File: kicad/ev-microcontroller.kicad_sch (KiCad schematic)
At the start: 0 parts

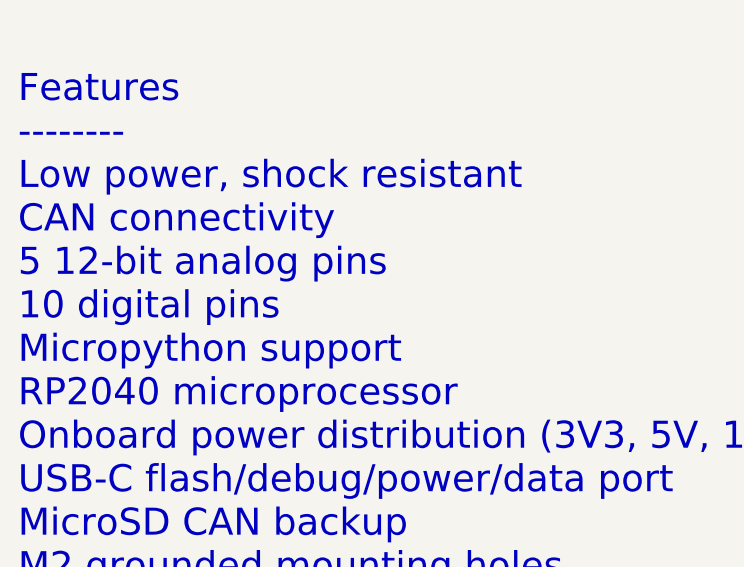
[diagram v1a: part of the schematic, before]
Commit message: Updated schematic with various changes
Increased size of small components
Updated title/spec sheet
Cleaned footprints
Other small changes as well
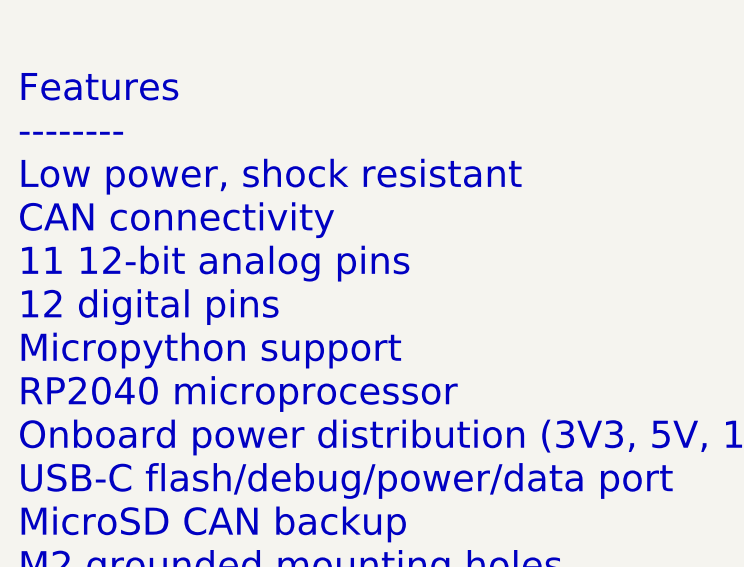
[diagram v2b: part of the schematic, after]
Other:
- note added: "Features -------- Low power, shock resistant CAN connectivity 11 12-bit analog pins 12 digital pins Micropython support RP2040 microprocessor Onboard power distribution (3V3, 5V, 12V) USB-C flash/debug/power/data port MicroSD CAN backup M2 grounded mounting holes Board thermistor 9 axis gyroscope Compact (30mm x 40mm) Electrical protections (overcurrent, undervoltage, etc.)"
- note removed: "Features -------- Low power, shock resistant CAN connectivity 5 12-bit analog pins 10 digital pins Micropython support RP2040 microprocessor Onboard power distribution (3V3, 5V, 12V) USB-C flash/debug/power/data port MicroSD CAN backup M2 grounded mounting holes Board thermistor 9 axis gyroscope Compact (30mm x 40mm) Electrical protections (overcurrent, undervoltage, etc.)"
